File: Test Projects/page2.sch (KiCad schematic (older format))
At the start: 21 parts, among them P12 COLUMNS, P7 ROWS, U2 Teensy_3.2, U26 SF-74HC595, U27 SF-74HC595, U4 SGTL5000, U5 SF-MicroSD-12term

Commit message: Continued proto 1 layout
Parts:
- removed JACK1: TRS_6term, SparkFun-Footprints:SF-Neutrik-Jack-6-term, symbol TRS_6term
- added P21: CONN_01X03, Pin_Headers:Pin_Header_Straight_1x03, symbol CONN_01X03
- P12: value COLUMNS -> COLS1
- P7: value ROWS -> COLS0
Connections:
- net at U4.2 (HPR): now also P21.2 (P2)
- net at U4.4 (HPVGND): now also P21.3 (P3)
- net at U4.6 (HPL): now also P21.1 (P1)
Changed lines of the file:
@@
-$EndComp
-$Comp
-L TRS_6term JACK1
-U 1 1 56871FC2
-P 7450 2900
-F 0 "JACK1" V 7750 2900 60  0000 C CNN
-F 1 "TRS_6term" V 7825 2900 60  0000 C CNN
-F 2 "SparkFun-Footprints:SF-Neutrik-Jack-6-term" H 7250 2700 60  0001 C CNN
-F 3 "" H 7250 2700 60  0000 C CNN
-	1    7450 2900
-	1    0    0    -1
 $EndComp
 $Comp
@@
 	5750 1350 5750 1900
 Wire Wire Line
-	6250 2950 7150 2950
-Wire Wire Line
-	6250 3050 6950 3050
-Wire Wire Line
-	6950 3050 6950 2750
-Wire Wire Line
-	6950 2750 7150 2750
-Wire Wire Line
-	6250 3150 7150 3150
+	6250 2950 6500 2950
+Wire Wire Line
+	6250 3050 6500 3050
+Wire Wire Line
+	6250 3150 6500 3150
 $Comp
 L GND #PWR018
@@
 P 2900 5450
 F 0 "P7" H 2900 5900 50  0000 C CNN
-F 1 "ROWS" V 3000 5450 50  0000 C CNN
+F 1 "COLS0" V 3000 5450 50  0000 C CNN
 F 2 "Pin_Headers:Pin_Header_Straight_1x08" H 2900 5450 50  0001 C CNN
 F 3 "" H 2900 5450 50  0000 C CNN
@@
 P 5650 5450
 F 0 "P12" H 5650 5900 50  0000 C CNN
-F 1 "COLUMNS" V 5750 5450 50  0000 C CNN
+F 1 "COLS1" V 5750 5450 50  0000 C CNN
 F 2 "Pin_Headers:Pin_Header_Straight_1x08" H 5650 5450 50  0001 C CNN
 F 3 "" H 5650 5450 50  0000 C CNN
@@
 Wire Wire Line
 	8550 3750 8450 3750
+$Comp
+L CONN_01X03 P21
+U 1 1 568AABAC
+P 6700 3050
+F 0 "P21" H 6700 3250 50  0000 C CNN
+F 1 "CONN_01X03" V 6800 3050 50  0000 C CNN
+F 2 "Pin_Headers:Pin_Header_Straight_1x03" H 6700 3050 50  0001 C CNN
+F 3 "" H 6700 3050 50  0000 C CNN
+	1    6700 3050
+	1    0    0    -1
+$EndComp
 $EndSCHEMATC

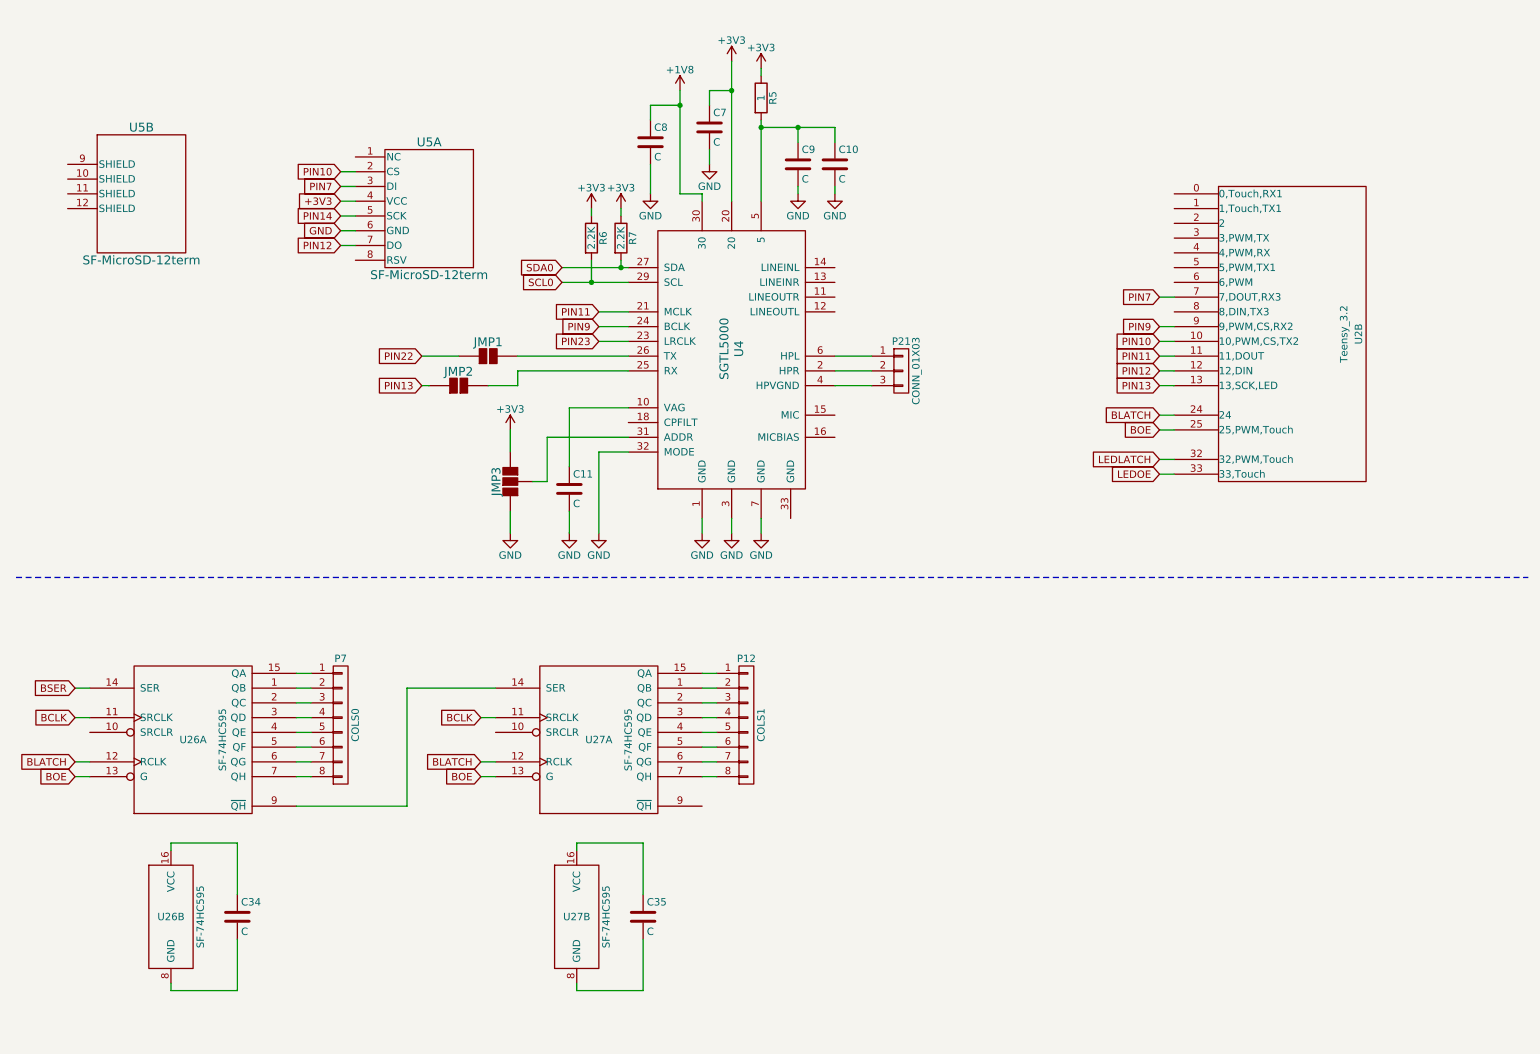
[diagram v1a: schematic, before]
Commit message: Moved to 10x5 size
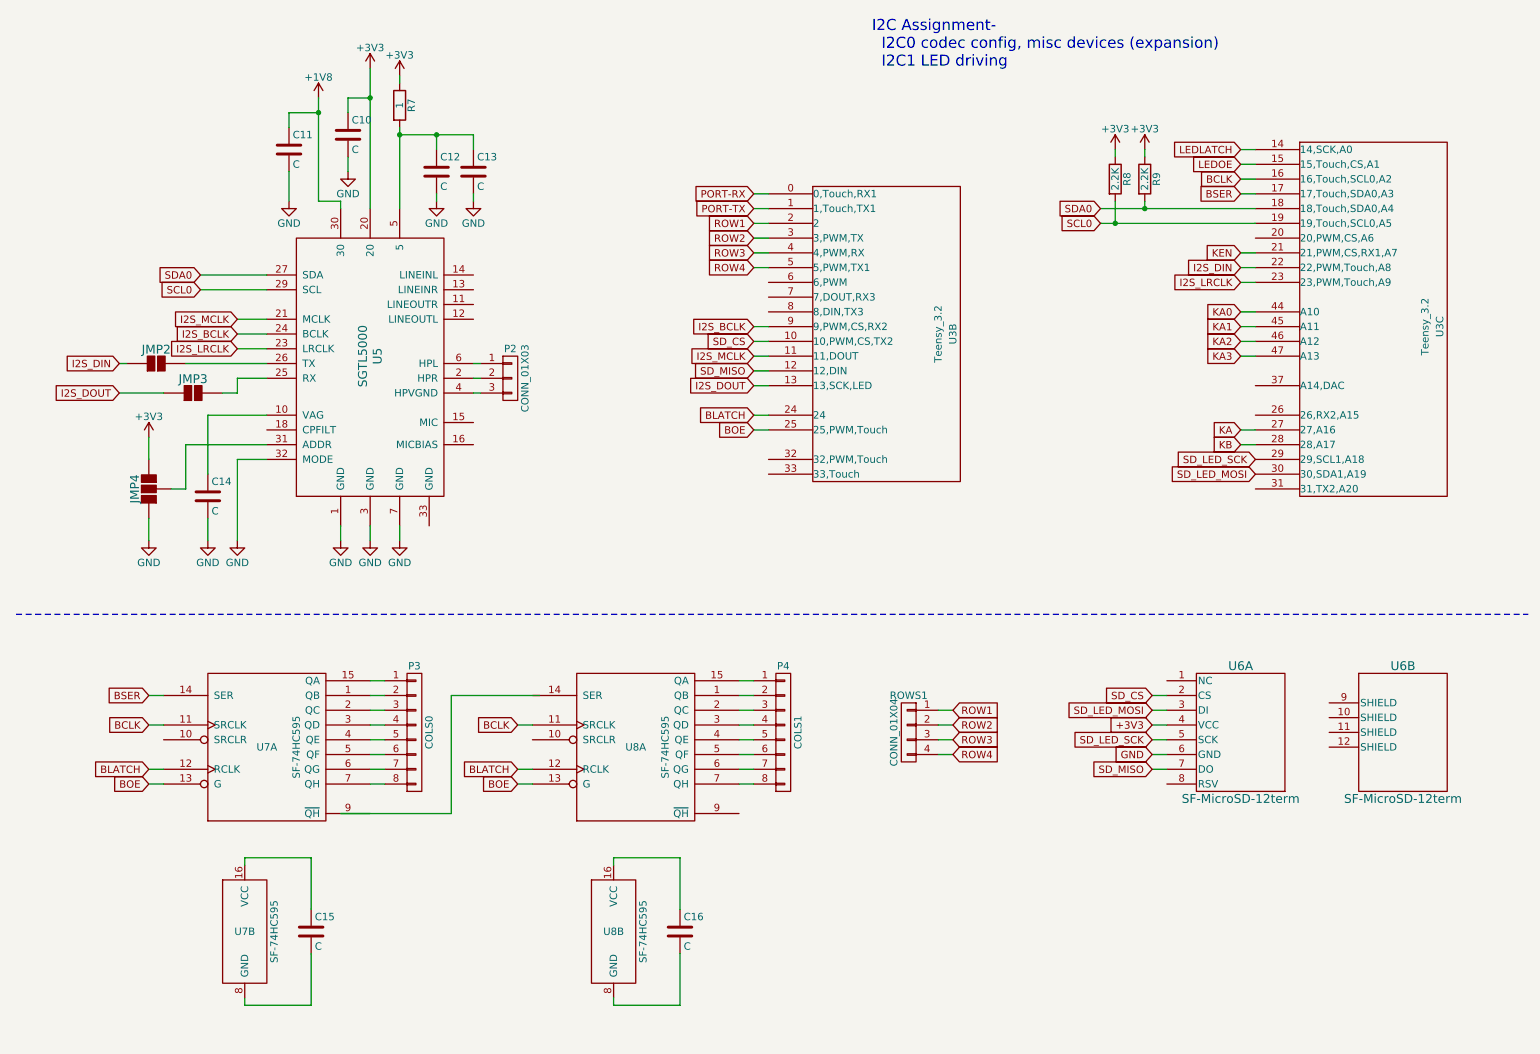
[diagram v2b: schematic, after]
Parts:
- removed R6, R7: 2.2K, Resistors_SMD:R_0603, symbol R
- added R8, R9: 2.2K, Resistors_SMD:R_0603, symbol R
- added ROWS1: CONN_01X04, Pin_Headers:Pin_Header_Straight_1x04, symbol CONN_01X04
- added unit 3 of U3
- renumbered C7 to C10, C8 to C11, C9 to C12, C10 to C13, C11 to C14, C34 to C15, C35 to C16, JMP1 to JMP2, JMP2 to JMP3, JMP3 to JMP4, P21 to P2, P7 to P3, P12 to P4, R5 to R7, U2 to U3, U4 to U5, U5 to U6, U26 to U7, U27 to U8
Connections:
- net +3V3: now also R8.1, R9.1
- net BCLK: now also U3.16 (16,Touch,SCL0,A2)
- net BSER: now also U3.17 (17,Touch,SDA0,A3)
- net LEDLATCH: now also U3.14 (14,SCK,A0); no longer U3.32 (32,PWM,Touch)
- net LEDOE: now also U3.15 (15,Touch,CS,A1); no longer U3.33 (33,Touch)
- net SCL0: now also R8.2, U3.19 (19,Touch,SCL0,A5)
- net SDA0: now also R9.2, U3.18 (18,Touch,SDA0,A4)
- net PORT-RX: now reaches U3.0 (0,Touch,RX1)
- net PORT-TX: now reaches U3.1 (1,Touch,TX1)
- net ROW1: now reaches U3.2
- net ROW1: now also ROWS1.1 (P1)
- net ROW2: now reaches U3.3 (3,PWM,TX)
- net ROW2: now also ROWS1.2 (P2)
- net ROW3: now reaches U3.4 (4,PWM,RX)
- net ROW3: now also ROWS1.3 (P3)
- net ROW4: now reaches U3.5 (5,PWM,TX1)
- net ROW4: now also ROWS1.4 (P4)
- net at U7.9 (~QH): no longer U8.14 (SER)
- net PIN10 renamed SD_CS
- net PIN11 renamed I2S_MCLK
- net PIN12 renamed SD_MISO
- net PIN13 renamed I2S_DOUT
- net PIN14 renamed SD_LED_SCK
- net SD_LED_SCK: now also U3.29 (29,SCL1,A18)
- net PIN22 renamed I2S_DIN
- net I2S_DIN: now also U3.22 (22,PWM,Touch,A8)
- net PIN23 renamed I2S_LRCLK
- net I2S_LRCLK: now also U3.23 (23,PWM,Touch,A9)
- net PIN7: no longer names the net of U3.7 (7,DOUT,RX3)
- net PIN7: no longer U6.3 (DI)
- net PIN9 renamed I2S_BCLK
- new net KA: U3.27 (27,A16)
- new net KA0: U3.44 (A10)
- new net KA1: U3.45 (A11)
- new net KA2: U3.46 (A12)
- new net KA3: U3.47 (A13)
- new net KB: U3.28 (28,A17)
- new net KEN: U3.21 (21,PWM,CS,RX1,A7)
- new net SD_LED_MOSI: U3.30 (30,SDA1,A19), U6.3 (DI)
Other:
- note added: "I2C Assignment-\n I2C0 codec config, misc devices (expansion)\n I2C1 LED driving\n"
- moved on the sheet: C10, C11, C12, C13, C14, C15, C16, JMP2, JMP3, JMP4, P2, P3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

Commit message: added second codec
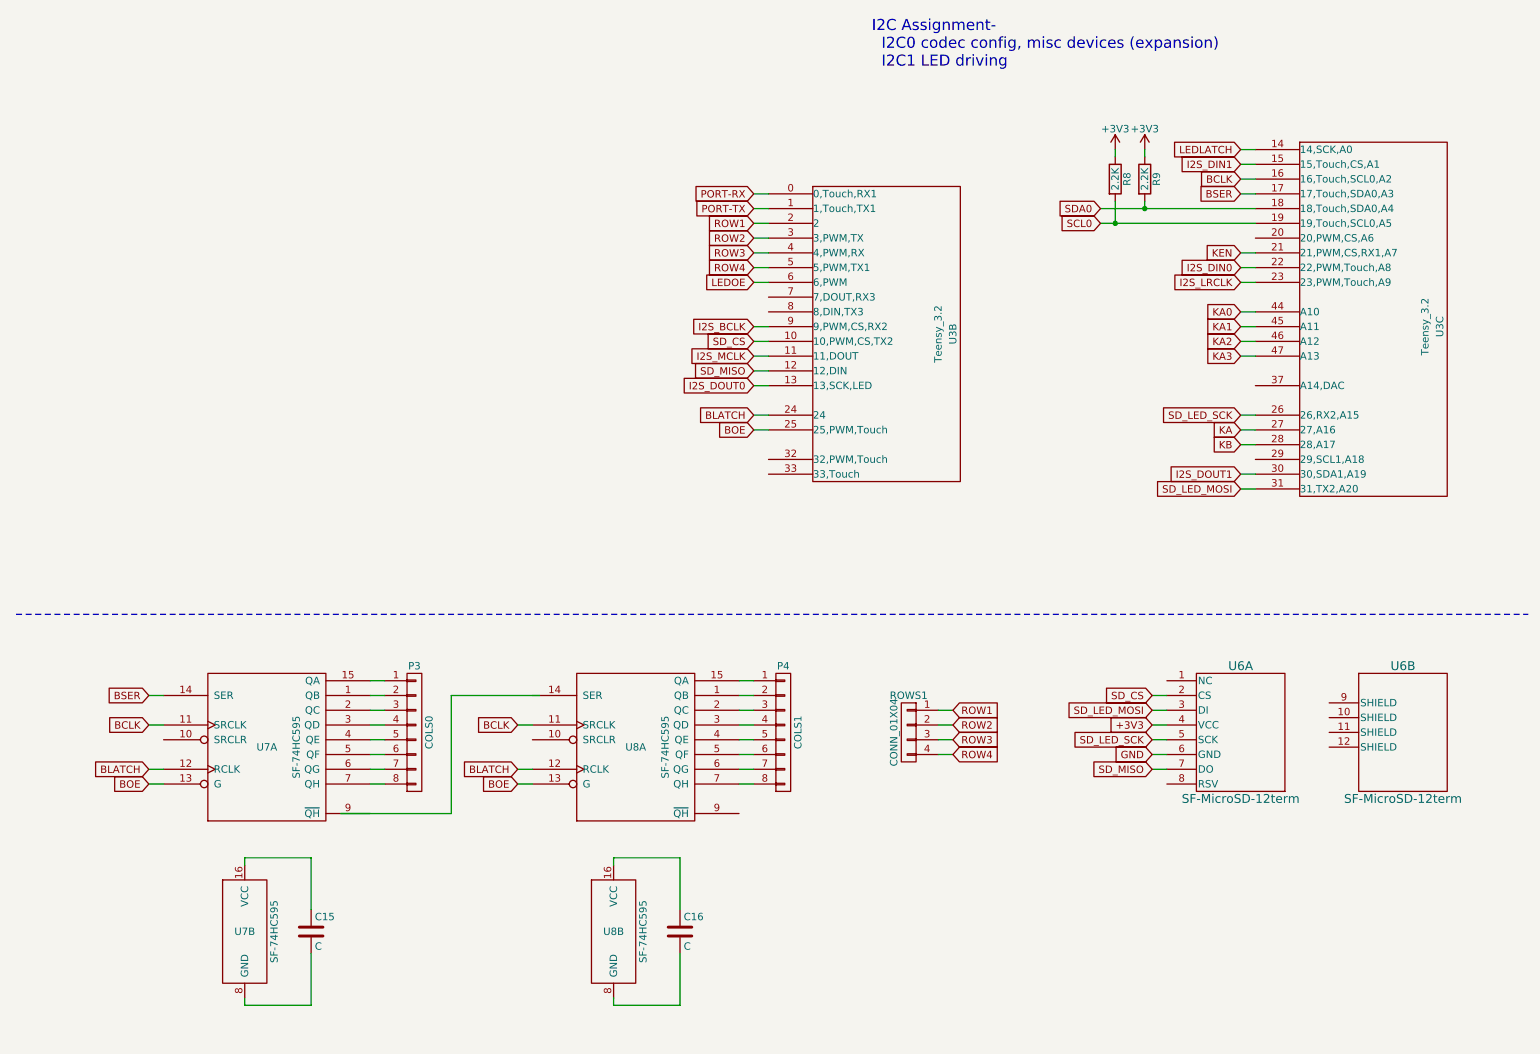
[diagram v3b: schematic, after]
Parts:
- removed C10, C11, C12, C13, C14: C, Capacitors_SMD:C_1206, symbol C
- removed JMP2, JMP3: 2Jumper, SparkFun-Footprints:SF-2way-open, symbol 2Jumper
- removed JMP4: 3Jumper, SparkFun-Footprints:SF-3way-open, symbol 3Jumper
- removed P2: CONN_01X03, Pin_Headers:Pin_Header_Straight_1x03, symbol CONN_01X03
- removed R7: 1, Resistors_SMD:R_0603, symbol R
- removed U5: SGTL5000, SparkFun-Footprints:SF-QFN-32-NXP-SGTL5000, symbol SGTL5000
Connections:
- net LEDOE: now also U3.6 (6,PWM); no longer U3.15 (15,Touch,CS,A1)
- net SD_LED_MOSI: now also U3.31 (31,TX2,A20); no longer U3.30 (30,SDA1,A19)
- net SD_LED_SCK: now also U3.26 (26,RX2,A15); no longer U3.29 (29,SCL1,A18)
- net I2S_DIN renamed I2S_DIN0
- net I2S_DOUT renamed I2S_DOUT0
- new net I2S_DIN1: U3.15 (15,Touch,CS,A1)
- new net I2S_DOUT1: U3.30 (30,SDA1,A19)

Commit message: First major routing pass
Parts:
- added C42: C, Capacitors_SMD:C_0603, symbol C
- added JMP8, JMP9: 2Jumper, SparkFun-Footprints:SF-2way-open, symbol 2Jumper
- added P31: PIN20, SparkFun-Footprints:Single_PTH, symbol CONN_01X01
- added P32: PIN8, SparkFun-Footprints:Single_PTH, symbol CONN_01X01
- added P33: SIO2, SparkFun-Footprints:Single_PTH, symbol CONN_01X01
- added P34: ~HOLD~/SIO3, SparkFun-Footprints:Single_PTH, symbol CONN_01X01
- added P35: PIN37, SparkFun-Footprints:Single_PTH, symbol CONN_01X01
- added P36: PIN29, SparkFun-Footprints:Single_PTH, symbol CONN_01X01
- added P37: PIN31, SparkFun-Footprints:Single_PTH, symbol CONN_01X01
- added U32: SPI_MEMORY_SOIC8, SparkFun-Footprints:SF-SOIC-8, symbol SPI_MEMORY_SOIC8
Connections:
- net +3V3: now also C15.1, C16.1, U7.10 (SRCLR), U7.16 (VCC), U8.10 (SRCLR), U8.16 (VCC), C42.1, JMP8.1, JMP9.1, U32.8 (VCC)
- net GND: now also C15.2, C16.2, U7.8 (GND), U8.8 (GND), C42.2, U32.4 (VSS)
- net LED_LATCH: now reaches U3.32 (32,PWM,Touch)
- net LED_OE: now reaches U3.33 (33,Touch)
- net SPI_MOSI: now reaches U3.7 (7,DOUT,RX3)
- net SPI_MOSI: now also U6.3 (DI), U32.5 (SI/SIO0)
- net at U3.8 (8,DIN,TX3): now also P32.1 (P1)
- net at U7.9 (~QH): now also U8.14 (SER)
- net at U3.20 (20,PWM,CS,A6): now also P31.1 (P1)
- net at U3.29 (29,SCL1,A18): now also P36.1 (P1)
- net at U3.37 (A14,DAC): now also P35.1 (P1)
- net LEDLATCH renamed SPI_SCK
- net SPI_SCK: now also U6.5 (SCK), U32.6 (SCK)
- net LEDOE renamed RAM_CS
- net RAM_CS: now also U32.1 (~CS)
- net SD_LED_MOSI: no longer names the net of U3.31 (31,TX2,A20)
- net SD_LED_MOSI: now also P37.1 (P1); no longer U6.3 (DI)
- net SD_LED_SCK renamed !LED_RST
- net !LED_RST: no longer U6.5 (SCK)
- net SD_MISO renamed SPI_MISO
- net SPI_MISO: now also U32.2 (SO/SIO1)
- new net: JMP8.2, P33.1 (P1), U32.3 (SIO2)
- new net: JMP9.2, P34.1 (P1), U32.7 (~HOLD~/SIO3)
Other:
- note added: "I2C Assignment-\n I2C0 codec config, misc devices (expansion)\nSPI\n SD card\n RAM/ROM\n LEDs\n"
- note removed: "I2C Assignment-\n I2C0 codec config, misc devices (expansion)\n I2C1 LED driving\n"
